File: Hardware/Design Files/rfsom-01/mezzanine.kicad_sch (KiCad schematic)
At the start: 5 parts, among them J3 Conn_01x06, J4 Conn_01x06, U15 FT232HQ-REEL

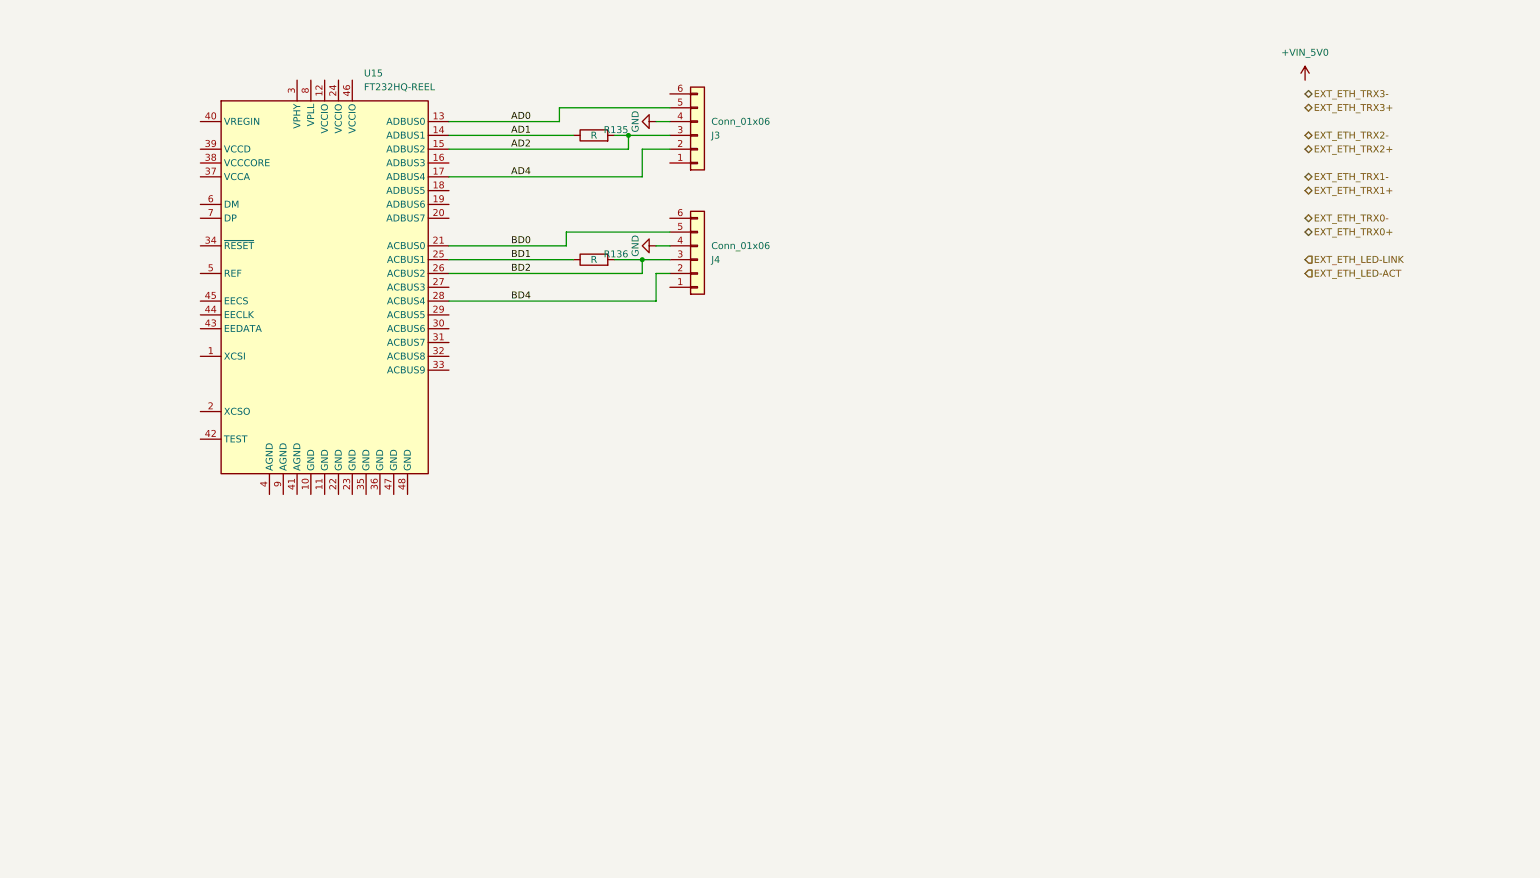
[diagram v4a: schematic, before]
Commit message: routing changes; added mezzanine; added pl ram;
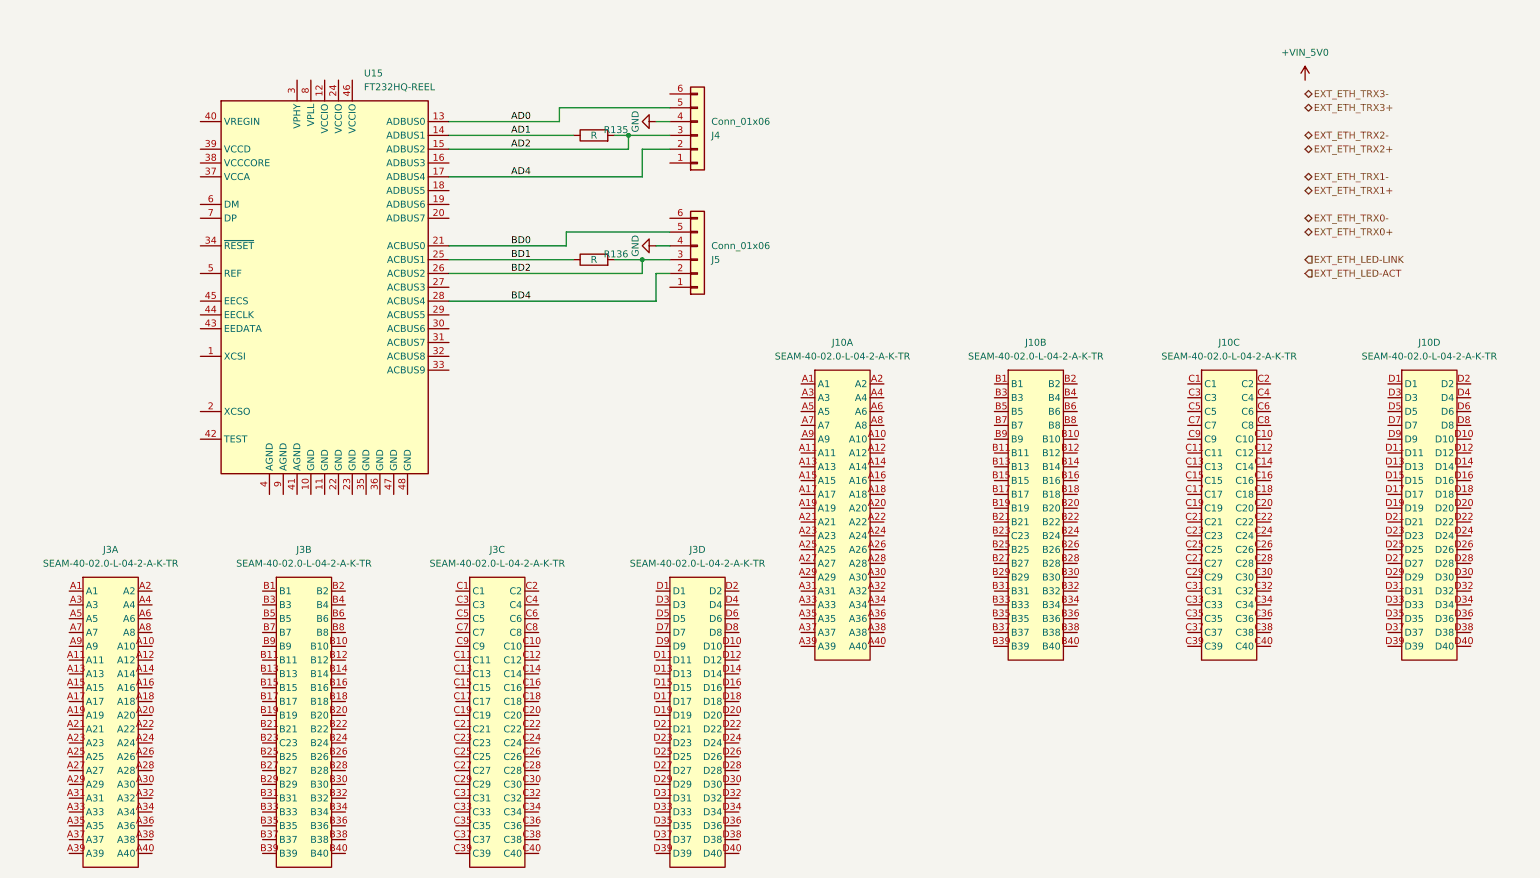
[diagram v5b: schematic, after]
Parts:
- added J10, J3: SEAM-40-02.0-L-04-2-A-K-TR, Connectors:SEAM-40-XX.X-XXX-04-X-A-XX-XX, symbol Connectors:SEAM-40-02.0-L-04-2-A-K-TR
- renumbered J3 to J4, J4 to J5

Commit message: updated sch pdf; routign progress;
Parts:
- removed J4, J5: Conn_01x06, symbol Connector_Generic:Conn_01x06
- removed R135, R136: R, symbol Device:R
- removed U15: FT232HQ-REEL, Package_DFN_QFN:QFN-48-1EP_7x7mm_P0.5mm_EP5.1x5.1mm, symbol Interface_USB:FT232H
